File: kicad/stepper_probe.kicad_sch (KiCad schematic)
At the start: 50 parts, among them J1 Conn_01x04_Male, J2 Conn_01x04_Male, J3 BAT, J4 Conn_01x03_Male, J5 SWD, J6 Reset header, M1 Motor, Q1 PJA3439, SW1 SW_Push, U1 CC6920BSO-5A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

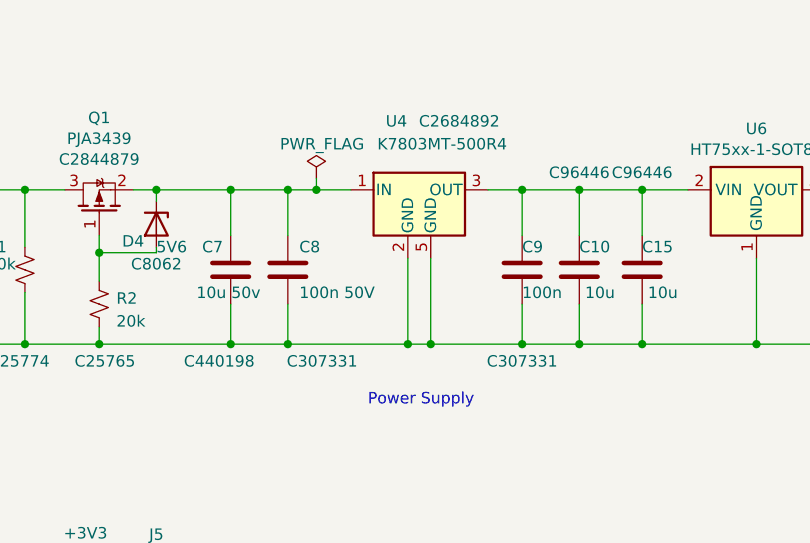
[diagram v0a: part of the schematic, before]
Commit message: Cleaned up kicad 6 files.
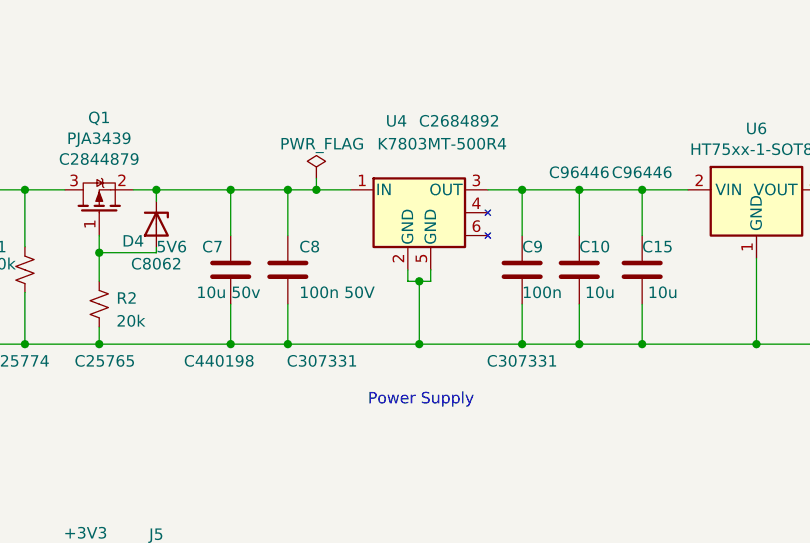
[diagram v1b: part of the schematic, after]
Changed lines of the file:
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@@
   (junction (at 50.165 144.145) (diameter 0) (color 0 0 0 0)
   )
-  (junction (at 205.105 53.975) (diameter 0) (color 0 0 0 0)
-  )
-  (junction (at 202.565 53.975) (diameter 0) (color 0 0 0 0)
-  )
   (junction (at 164.465 135.89) (diameter 0) (color 0 0 0 0)
   )
@@
   (junction (at 160.02 36.83) (diameter 0) (color 0 0 0 0)
   )
+  (junction (at 203.835 53.975) (diameter 0) (color 0 0 0 0)
+  )
   (junction (at 215.265 53.975) (diameter 0) (color 0 0 0 0)
   )
   (junction (at 192.405 36.83) (diameter 0) (color 0 0 0 0)
+  )
+  (junction (at 203.835 46.99) (diameter 0) (color 0 0 0 0)
   )
   (junction (at 25.4 135.255) (diameter 0) (color 0 0 0 0)
@@
     (stroke (width 0) (type default) (color 0 0 0 0))
   )
-  (wire (pts (xy 205.105 44.45) (xy 205.105 53.975))
-    (stroke (width 0) (type default) (color 0 0 0 0))
-  )
   (wire (pts (xy 79.375 55.88) (xy 81.28 55.88))
     (stroke (width 0) (type default) (color 0 0 0 0))
@@
     (stroke (width 0) (type default) (color 0 0 0 0))
   )
+  (wire (pts (xy 202.565 46.99) (xy 203.835 46.99))
+    (stroke (width 0) (type default) (color 0 0 0 0))
+  )
   (wire (pts (xy 55.88 62.865) (xy 54.61 62.865))
     (stroke (width 0) (type default) (color 0 0 0 0))
@@
     (stroke (width 0) (type default) (color 0 0 0 0))
   )
-  (wire (pts (xy 189.23 53.975) (xy 202.565 53.975))
-    (stroke (width 0) (type default) (color 0 0 0 0))
-  )
   (wire (pts (xy 165.735 135.89) (xy 164.465 135.89))
     (stroke (width 0) (type default) (color 0 0 0 0))
   )
-  (wire (pts (xy 202.565 53.975) (xy 205.105 53.975))
+  (wire (pts (xy 189.23 53.975) (xy 203.835 53.975))
+    (stroke (width 0) (type default) (color 0 0 0 0))
+  )
+  (wire (pts (xy 202.565 45.72) (xy 202.565 46.99))
     (stroke (width 0) (type default) (color 0 0 0 0))
   )
@@
   )
   (wire (pts (xy 260.35 53.34) (xy 260.35 53.975))
+    (stroke (width 0) (type default) (color 0 0 0 0))
+  )
+  (wire (pts (xy 203.835 53.975) (xy 215.265 53.975))
     (stroke (width 0) (type default) (color 0 0 0 0))
   )
@@
     (stroke (width 0) (type default) (color 0 0 0 0))
   )
+  (wire (pts (xy 203.835 46.99) (xy 203.835 53.975))
+    (stroke (width 0) (type default) (color 0 0 0 0))
+  )
   (wire (pts (xy 125.095 135.255) (xy 125.095 135.89))
     (stroke (width 0) (type default) (color 0 0 0 0))
@@
     (stroke (width 0.1016) (type solid) (color 0 0 0 0))
   )
-  (wire (pts (xy 202.565 44.45) (xy 202.565 53.975))
-    (stroke (width 0) (type default) (color 0 0 0 0))
-  )
   (wire (pts (xy 248.92 36.83) (xy 252.095 36.83))
     (stroke (width 0) (type default) (color 0 0 0 0))
@@
     (stroke (width 0) (type default) (color 0 0 0 0))
   )
-  (wire (pts (xy 205.105 53.975) (xy 215.265 53.975))
-    (stroke (width 0) (type default) (color 0 0 0 0))
-  )
   (wire (pts (xy 50.165 144.145) (xy 50.165 145.415))
     (stroke (width 0) (type default) (color 0 0 0 0))
@@
     (stroke (width 0) (type default) (color 0 0 0 0))
   )
+  (wire (pts (xy 203.835 46.99) (xy 205.105 46.99))
+    (stroke (width 0) (type default) (color 0 0 0 0))
+  )
   (wire (pts (xy 96.52 28.575) (xy 94.615 28.575))
     (stroke (width 0) (type default) (color 0 0 0 0))
@@
   )
   (wire (pts (xy 86.995 155.575) (xy 86.995 163.83))
+    (stroke (width 0) (type default) (color 0 0 0 0))
+  )
+  (wire (pts (xy 205.105 46.99) (xy 205.105 45.72))
     (stroke (width 0) (type default) (color 0 0 0 0))
   )
@@
     (pin "2")
     (pin "3")
+    (pin "4")
     (pin "5")
+    (pin "6")
   )
   (symbol (lib_id "stepper_probe:GND") (at 239.395 142.24 0) (unit 1)
